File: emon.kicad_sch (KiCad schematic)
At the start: 34 parts, among them J1 Screw_Terminal_01x02, J2 Conn_01x03_MountingPin, J3 USB_C_Receptacle_PowerOnly_6P, SW1 RESET, SW2 BOOTSEL, U1 RAK3172-T-8-SM-I, U2 BME690, U3 BQ25185

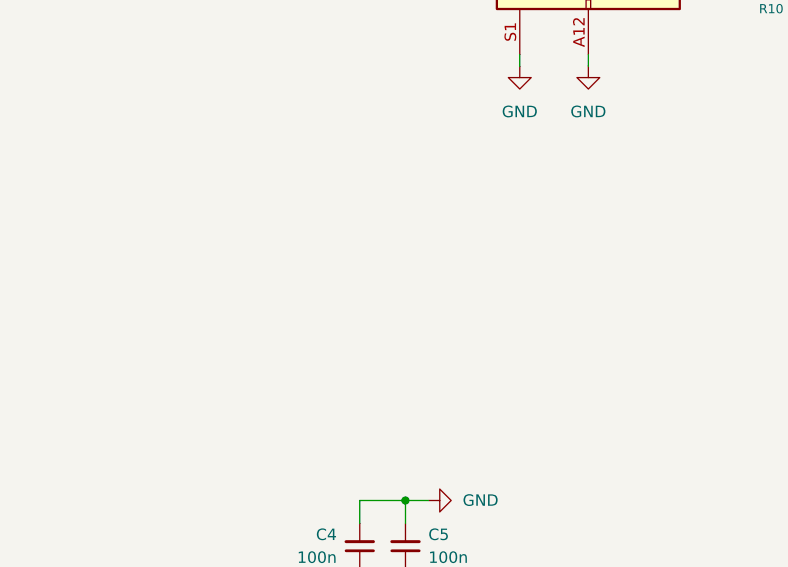
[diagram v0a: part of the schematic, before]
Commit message: finish schematic, start layout
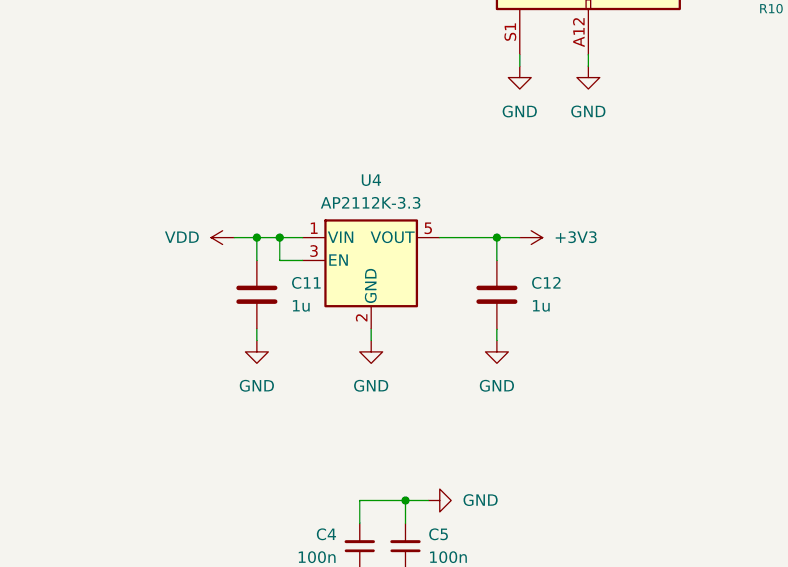
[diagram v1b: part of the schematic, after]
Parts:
- added C11, C12: 1u, Capacitor_SMD:C_0603_1608Metric_Pad1.08x0.95mm_HandSolder, symbol Device:C
- added U4: AP2112K-3.3, Package_TO_SOT_SMD:SOT-23-5_HandSoldering, symbol Regulator_Linear:AP2112K-3.3
- C1, C4, C5, C9: footprint (none) -> Capacitor_SMD:C_0201_0603Metric
- C10, C2, C6: footprint (none) -> Capacitor_SMD:C_0603_1608Metric
- C7, C8: footprint (none) -> Capacitor_SMD:C_0402_1005Metric
- D1: footprint (none) -> LED_SMD:LED_0603_1608Metric; MPN (none) -> LTST-C191KRKT
- D2: footprint (none) -> LED_SMD:LED_0603_1608Metric; MPN (none) -> LTST-C191KFKT
- H1, H2, H3, H4: footprint MountingHole:MountingHole_2.7mm_M2.5_ISO7380_Pad -> MountingHole:MountingHole_2.7mm_M2.5_ISO14580_Pad
- J3: footprint Connector_USB:USB_C_Receptacle_GCT_USB4135-GF-A_6P_TopMnt_Horizontal -> Connector_USB:USB_C_Receptacle_GCT_USB4125-xx-x_6P_TopMnt_Horizontal; MPN (none) -> USB4125-GF-A
- R1, R10, R12, R2, R3, R4, R5, R6, R7, R8, R9: footprint (none) -> Resistor_SMD:R_0201_0603Metric
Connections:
- net +3V3: now also C12.1, U4.5 (VOUT)
- net GND: now also C11.2, C12.2, U4.2 (GND)
- net VDD: now also C11.1, U4.1 (VIN), U4.3 (EN)

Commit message: layout progress
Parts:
- added J4: Conn_01x02_MountingPin, Connector_JST:JST_PH_S2B-PH-SM4-TB_1x02-1MP_P2.00mm_Horizontal, symbol Connector_Generic_MountingPin:Conn_01x02_MountingPin
- C6: footprint Capacitor_SMD:C_0603_1608Metric -> Capacitor_SMD:C_0402_1005Metric
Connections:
- net +BATT: now also J4.1 (Pin_1)
- net GND: now also U3.11 (GND), J4.2 (Pin_2), J4.MP (MountPin)
